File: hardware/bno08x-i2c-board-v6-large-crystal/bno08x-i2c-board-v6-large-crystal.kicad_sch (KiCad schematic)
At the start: 13 parts, among them J1 PIN_SDA, J2 PIN_SCL, J3 PIN_3V3, J4 PIN_GND

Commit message: v6
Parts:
- added C3, C5: 22pF, Capacitor_SMD:C_0402_1005Metric, symbol Device:C_Small
- added Y1: 32.768kHz, Crystal:Crystal_SMD_MicroCrystal_CM9V-T1A-2Pin_1.6x1.0mm, symbol Device:Crystal_Small
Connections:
- net +3.3V: no longer U1.10 (CLKSEL0)
- net GND: now also U1.10 (CLKSEL0), C3.2, C5.2; no longer U1.26 (XOUT32/CLKSEL1)
- net XIN32: now reaches U1.27 (XIN32)
- net XIN32: now also C3.1, Y1.1
- new net CLKSEL1: C5.1, U1.26 (XOUT32/CLKSEL1), Y1.2
- no-connect marks 4 -> 3

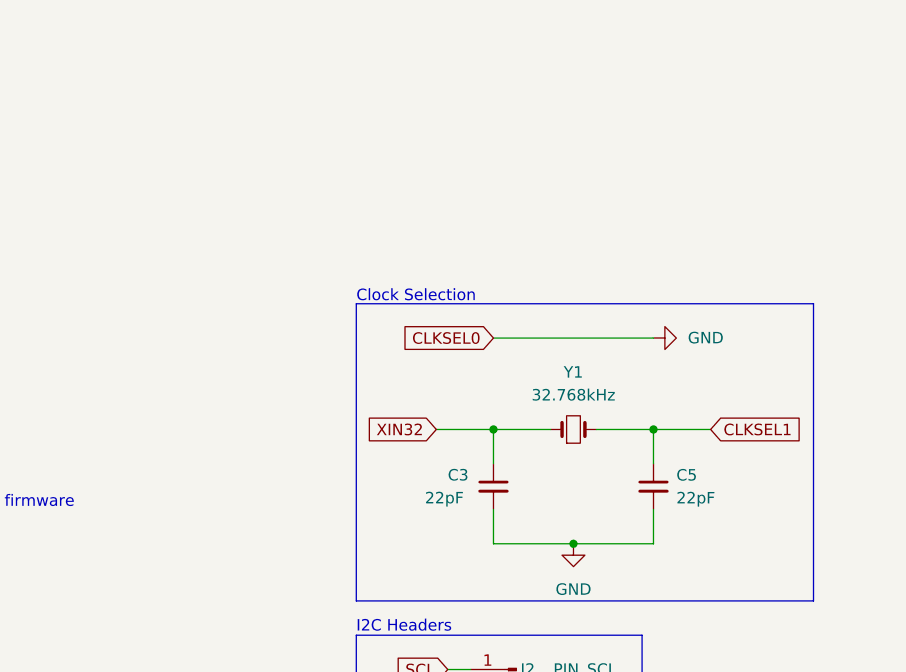
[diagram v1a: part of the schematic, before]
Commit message: change cap size
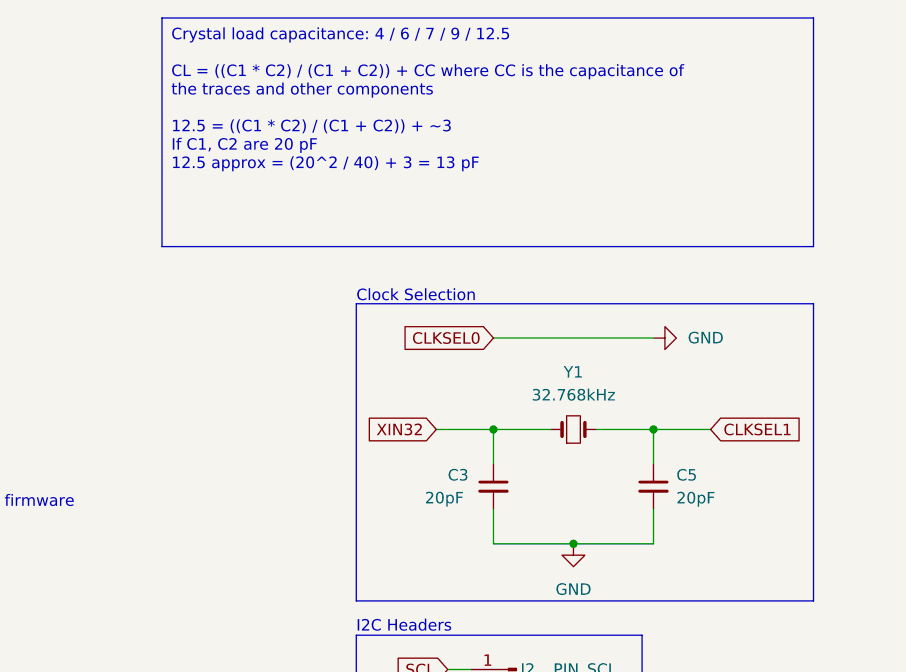
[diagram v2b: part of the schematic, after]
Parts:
- C3, C5: value 22pF -> 20pF
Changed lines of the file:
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@@
     (fill (type none))
+  )
+  (text_box "Crystal load capacitance: 4 / 6 / 7 / 9 / 12.5\n\nCL = ((C1 * C2) / (C1 + C2)) + CC where CC is the capacitance of the traces and other components\n\n12.5 = ((C1 * C2) / (C1 + C2)) + ~3\nIf C1, C2 are 20 pF\n12.5 approx = (20^2 / 40) + 3 = 13 pF"
+    (at 204.47 17.78 0) (size 72.39 25.4)
+    (stroke (width 0) (type default))
+    (fill (type none))
+    (effects (font (size 1.27 1.27)) (justify left top))
   )
   (text_box "For I2C the PS pins should be as follows:\n- PS0 Low\n- PS1 Low\n\nFor external clock selection the CLKSEL pins should be as follows:\n- CLKSEL0 Low\n- CLKSEL1 connected to crystal"
@@
         )
       )
-      (project "bno08x-i2c-board-v6-large"
+      (project "bno08x-i2c-board-v6-large-crystal"
         (path "/d7bfa7c2-2653-4e07-b133-5c72cde0b07d"
           (reference "#FLG01") (unit 1)
@@
         )
       )
-      (project "bno08x-i2c-board-v6-large"
+      (project "bno08x-i2c-board-v6-large-crystal"
         (path "/d7bfa7c2-2653-4e07-b133-5c72cde0b07d"
           (reference "R4") (unit 1)
@@
         )
       )
-      (project "bno08x-i2c-board-v6-large"
+      (project "bno08x-i2c-board-v6-large-crystal"
         (path "/d7bfa7c2-2653-4e07-b133-5c72cde0b07d"
           (reference "R1") (unit 1)
@@
       (effects (font (size 1.27 1.27)) (justify left))
     )
-    (property "Value" "22pF" (at 233.68 71.12 0)
+    (property "Value" "20pF" (at 233.68 71.12 0)
       (effects (font (size 1.27 1.27)) (justify left))
     )
@@
     (pin "2")
     (instances
-      (project "bno08x-i2c-board-v6-large"
+      (project "bno08x-i2c-board-v6-large-crystal"
         (path "/d7bfa7c2-2653-4e07-b133-5c72cde0b07d"
           (reference "C3") (unit 1)
@@
         )
       )
-      (project "bno08x-i2c-board-v6-large"
+      (project "bno08x-i2c-board-v6-large-crystal"
         (path "/d7bfa7c2-2653-4e07-b133-5c72cde0b07d"
           (reference "#PWR07") (unit 1)
@@
         )
       )
-      (project "bno08x-i2c-board-v6-large"
+      (project "bno08x-i2c-board-v6-large-crystal"
         (path "/d7bfa7c2-2653-4e07-b133-5c72cde0b07d"
           (reference "R3") (unit 1)
@@
       (effects (font (size 1.27 1.27)) (justify left))
     )
-    (property "Value" "22pF" (at 261.62 71.1263 0)
+    (property "Value" "20pF" (at 261.62 71.1263 0)
       (effects (font (size 1.27 1.27)) (justify left))
     )
@@
     (pin "2")
     (instances
-      (project "bno08x-i2c-board-v6-large"
+      (project "bno08x-i2c-board-v6-large-crystal"
         (path "/d7bfa7c2-2653-4e07-b133-5c72cde0b07d"
           (reference "C5") (unit 1)
@@
         )
       )
-      (project "bno08x-i2c-board-v6-large"
+      (project "bno08x-i2c-board-v6-large-crystal"
         (path "/d7bfa7c2-2653-4e07-b133-5c72cde0b07d"
           (reference "C2") (unit 1)
@@
         )
       )
-      (project "bno08x-i2c-board-v6-large"
+      (project "bno08x-i2c-board-v6-large-crystal"
         (path "/d7bfa7c2-2653-4e07-b133-5c72cde0b07d"
           (reference "#PWR08") (unit 1)
@@
         )
       )
-      (project "bno08x-i2c-board-v6-large"
+      (project "bno08x-i2c-board-v6-large-crystal"
         (path "/d7bfa7c2-2653-4e07-b133-5c72cde0b07d"
           (reference "#PWR05") (unit 1)
@@
         )
       )
-      (project "bno08x-i2c-board-v6-large"
+      (project "bno08x-i2c-board-v6-large-crystal"
         (path "/d7bfa7c2-2653-4e07-b133-5c72cde0b07d"
           (reference "#PWR06") (unit 1)
@@
         )
       )
-      (project "bno08x-i2c-board-v6-large"
+      (project "bno08x-i2c-board-v6-large-crystal"
         (path "/d7bfa7c2-2653-4e07-b133-5c72cde0b07d"
           (reference "#PWR016") (unit 1)
@@
     (pin "1")
     (instances
-      (project "bno08x-i2c-board-v6-large"
+      (project "bno08x-i2c-board-v6-large-crystal"
         (path "/d7bfa7c2-2653-4e07-b133-5c72cde0b07d"
           (reference "#PWR020") (unit 1)
@@
         )
       )
-      (project "bno08x-i2c-board-v6-large"
+      (project "bno08x-i2c-board-v6-large-crystal"
         (path "/d7bfa7c2-2653-4e07-b133-5c72cde0b07d"
           (reference "U1") (unit 1)
@@
         )
       )
-      (project "bno08x-i2c-board-v6-large"
+      (project "bno08x-i2c-board-v6-large-crystal"
         (path "/d7bfa7c2-2653-4e07-b133-5c72cde0b07d"
           (reference "J1") (unit 1)
@@
         )
       )
-      (project "bno08x-i2c-board-v6-large"
+      (project "bno08x-i2c-board-v6-large-crystal"
         (path "/d7bfa7c2-2653-4e07-b133-5c72cde0b07d"
           (reference "#PWR018") (unit 1)
@@
         )
       )
-      (project "bno08x-i2c-board-v6-large"
+      (project "bno08x-i2c-board-v6-large-crystal"
         (path "/d7bfa7c2-2653-4e07-b133-5c72cde0b07d"
           (reference "#PWR04") (unit 1)
@@
         )
       )
-      (project "bno08x-i2c-board-v6-large"
+      (project "bno08x-i2c-board-v6-large-crystal"
         (path "/d7bfa7c2-2653-4e07-b133-5c72cde0b07d"
           (reference "C1") (unit 1)
@@
         )
       )
-      (project "bno08x-i2c-board-v6-large"
+      (project "bno08x-i2c-board-v6-large-crystal"
         (path "/d7bfa7c2-2653-4e07-b133-5c72cde0b07d"
           (reference "#PWR02") (unit 1)
@@
         )
       )
-      (project "bno08x-i2c-board-v6-large"
+      (project "bno08x-i2c-board-v6-large-crystal"
         (path "/d7bfa7c2-2653-4e07-b133-5c72cde0b07d"
           (reference "J4") (unit 1)
@@
         )
       )
-      (project "bno08x-i2c-board-v6-large"
+      (project "bno08x-i2c-board-v6-large-crystal"
         (path "/d7bfa7c2-2653-4e07-b133-5c72cde0b07d"
           (reference "#PWR09") (unit 1)
@@
         )
       )
-      (project "bno08x-i2c-board-v6-large"
+      (project "bno08x-i2c-board-v6-large-crystal"
         (path "/d7bfa7c2-2653-4e07-b133-5c72cde0b07d"
           (reference "#PWR014") (unit 1)
@@
         )
       )
-      (project "bno08x-i2c-board-v6-large"
+      (project "bno08x-i2c-board-v6-large-crystal"
         (path "/d7bfa7c2-2653-4e07-b133-5c72cde0b07d"
           (reference "#PWR011") (unit 1)
@@
         )
       )
-      (project "bno08x-i2c-board-v6-large"
+      (project "bno08x-i2c-board-v6-large-crystal"
         (path "/d7bfa7c2-2653-4e07-b133-5c72cde0b07d"
           (reference "J2") (unit 1)
@@
     (pin "1")
     (instances
-      (project "bno08x-i2c-board-v6-large"
+      (project "bno08x-i2c-board-v6-large-crystal"
         (path "/d7bfa7c2-2653-4e07-b133-5c72cde0b07d"
           (reference "#PWR019") (unit 1)
@@
         )
       )
-      (project "bno08x-i2c-board-v6-large"
+      (project "bno08x-i2c-board-v6-large-crystal"
         (path "/d7bfa7c2-2653-4e07-b133-5c72cde0b07d"
           (reference "#PWR013") (unit 1)
@@
     (pin "2")
     (instances
-      (project "bno08x-i2c-board-v6-large"
+      (project "bno08x-i2c-board-v6-large-crystal"
         (path "/d7bfa7c2-2653-4e07-b133-5c72cde0b07d"
           (reference "Y1") (unit 1)
@@
         )
       )
-      (project "bno08x-i2c-board-v6-large"
+      (project "bno08x-i2c-board-v6-large-crystal"
         (path "/d7bfa7c2-2653-4e07-b133-5c72cde0b07d"
           (reference "#PWR010") (unit 1)
@@
         )
       )
-      (project "bno08x-i2c-board-v6-large"
+      (project "bno08x-i2c-board-v6-large-crystal"
         (path "/d7bfa7c2-2653-4e07-b133-5c72cde0b07d"
           (reference "C4") (unit 1)
@@
         )
       )
-      (project "bno08x-i2c-board-v6-large"
+      (project "bno08x-i2c-board-v6-large-crystal"
         (path "/d7bfa7c2-2653-4e07-b133-5c72cde0b07d"
           (reference "#PWR017") (unit 1)
@@
         )
       )
-      (project "bno08x-i2c-board-v6-large"
+      (project "bno08x-i2c-board-v6-large-crystal"
         (path "/d7bfa7c2-2653-4e07-b133-5c72cde0b07d"
           (reference "R5") (unit 1)
@@
         )
       )
-      (project "bno08x-i2c-board-v6-large"
+      (project "bno08x-i2c-board-v6-large-crystal"
         (path "/d7bfa7c2-2653-4e07-b133-5c72cde0b07d"
           (reference "#PWR012") (unit 1)
@@
         )
       )
-      (project "bno08x-i2c-board-v6-large"
+      (project "bno08x-i2c-board-v6-large-crystal"
         (path "/d7bfa7c2-2653-4e07-b133-5c72cde0b07d"
           (reference "#PWR01") (unit 1)
@@
         )
       )
-      (project "bno08x-i2c-board-v6-large"
+      (project "bno08x-i2c-board-v6-large-crystal"
         (path "/d7bfa7c2-2653-4e07-b133-5c72cde0b07d"
           (reference "R2") (unit 1)
@@
         )
       )
-      (project "bno08x-i2c-board-v6-large"
+      (project "bno08x-i2c-board-v6-large-crystal"
         (path "/d7bfa7c2-2653-4e07-b133-5c72cde0b07d"
           (reference "#PWR015") (unit 1)
@@
         )
       )
-      (project "bno08x-i2c-board-v6-large"
+      (project "bno08x-i2c-board-v6-large-crystal"
         (path "/d7bfa7c2-2653-4e07-b133-5c72cde0b07d"
           (reference "J3") (unit 1)
@@
         )
       )
-      (project "bno08x-i2c-board-v6-large"
+      (project "bno08x-i2c-board-v6-large-crystal"
         (path "/d7bfa7c2-2653-4e07-b133-5c72cde0b07d"
           (reference "#PWR03") (unit 1)
